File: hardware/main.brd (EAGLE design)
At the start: 95.2 x 80.4 mm, 96 parts, among them IC1 MPU-6050, IC2 TB6612FNG, M1 MOTOR_MOUNT_V2, M2 LED_MOUNT, M3 LED_MOUNT, M4 LED_MOUNT, M5 LED_MOUNT, M6 LED_MOUNT, M7 LED_MOUNT, Q7 IRLML2244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

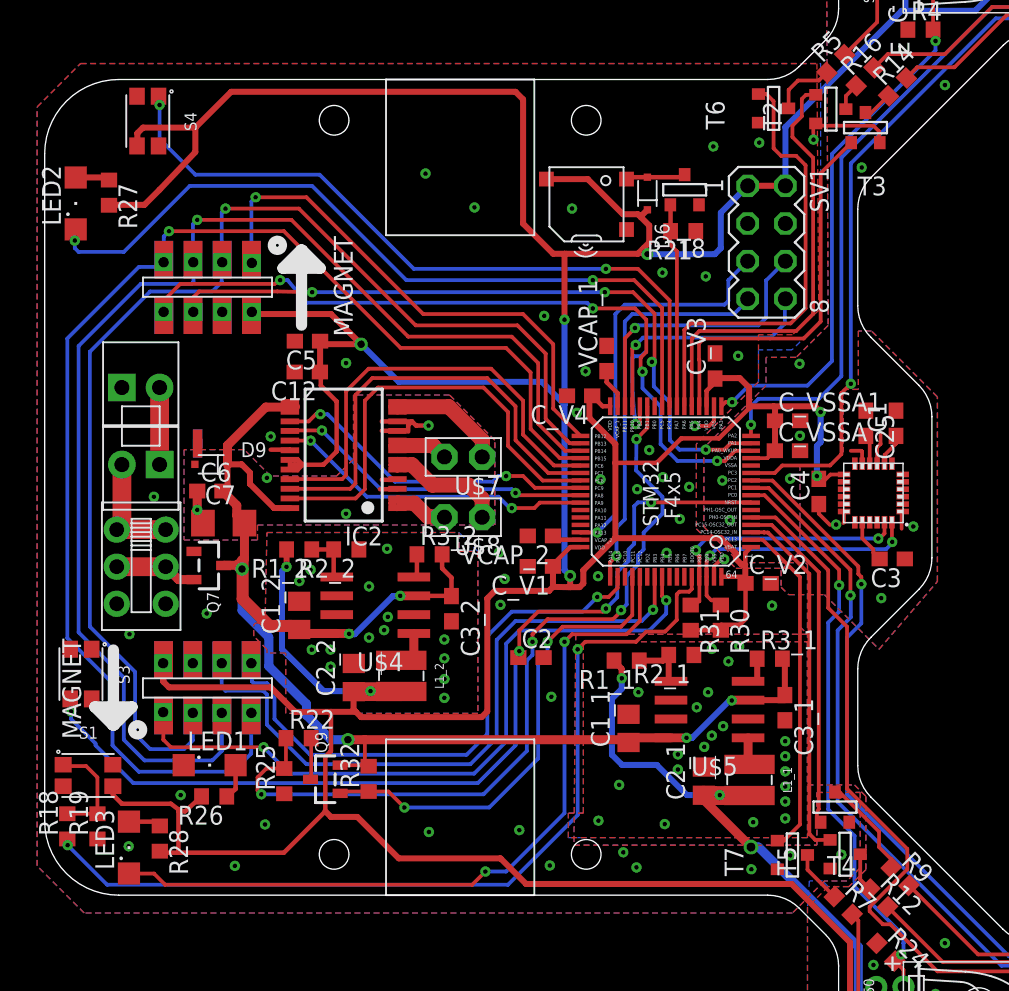
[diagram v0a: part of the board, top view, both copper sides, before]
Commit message: dodanie lini od przerwania od MPU, dodanie C na DCDC 3V3, laczenie GNDA GND i GNDM, dodanie diod ESD na programator, rewizja
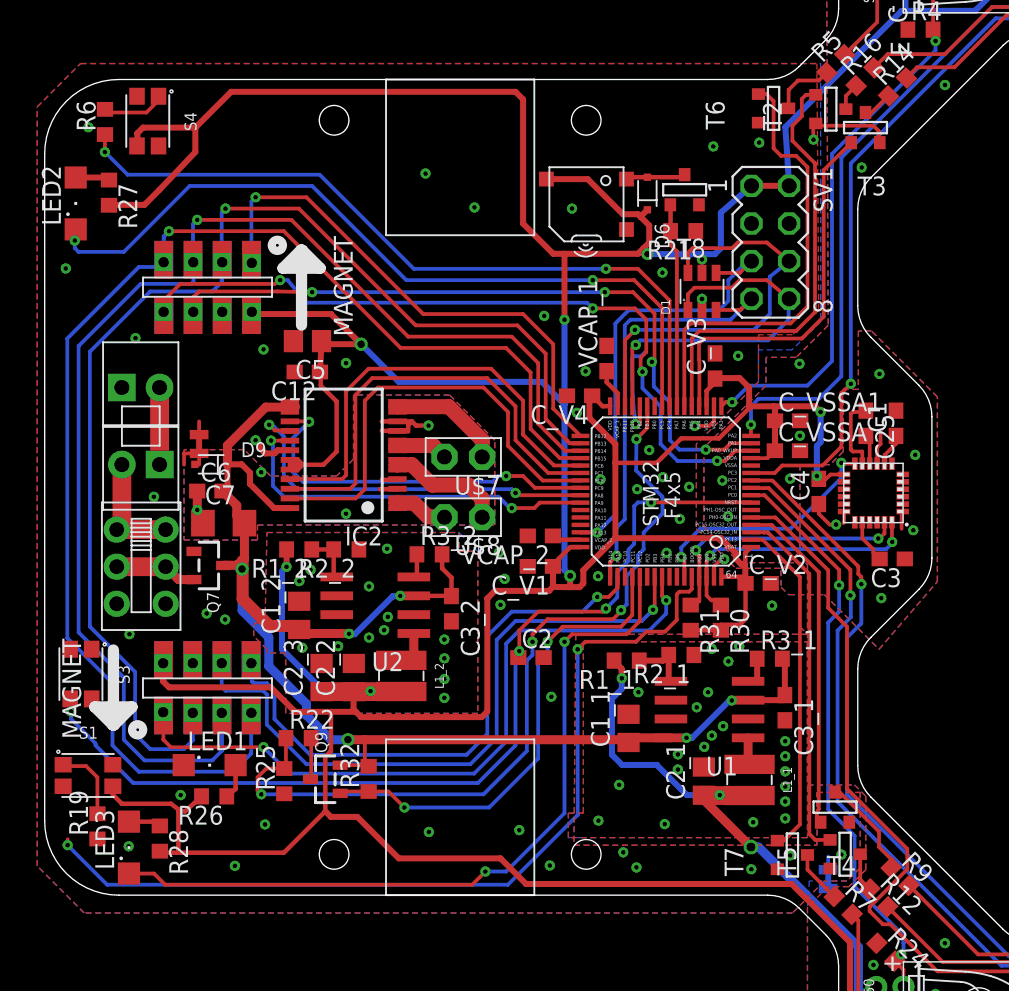
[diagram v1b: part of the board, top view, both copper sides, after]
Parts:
- removed R18: 1k, rcl:R0603
- removed U$1: GND_CONN, micromouse:GND_CONN
- added C2_3: 10u, rcl:C0805
- added D1: WE-TVS_824015, EAGLE-POWER_MAGNETICS-rev17a:WE-TVS_SOT23-6L
- added PT1, PT2: 2PT_GND_TIE, SparkFun-Passives:2PT_GND_TIE
- added R6: 1k, rcl:R0603
- C4: value 2,2n -> 100nF
- C5: device rcl:C0603 -> rcl:C0805
- moved SV1 0.25 mm to (48.9, 16.5)
- renumbered U$4 to U2, U$5 to U1, U$6 to U3
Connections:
- removed net N$23: R18.2, R19.2, S1.1
- removed net N$36: IC1.12
- removed net OSC_OUT: U3.PH1
- new net MPU_INT: IC1.12, U3.PB7
- new net N$25: R6.2, S4.1
- net +3V3: now also C2_3.1, D1.5
- net AGND: now also PT1.P$1
- net BOOT0: now also R19.2, S1.1; no longer R18.1
- net BTN1: now also R6.1; no longer S4.1
- net GND: now also C2_3.2, D1.2, PT1.P$2, PT2.P$1; no longer U$1.AGND, U$1.ANGD1
- net GNDA: now also PT2.P$2; no longer U$1.GND, U$1.GND1
- net SWCLK: now also D1.3
- net SWDIO: now also D1.4
- net USART3_RX: now also D1.6
- net USART3_TX: now also D1.1
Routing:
- net MPU_INT: track 0.00 -> 16.7 mm, vias 0 -> 2
- net USART3_TX: track 16.7 -> 25.8 mm
- net USART3_RX: track 19.0 -> 28.1 mm
- net GND: track 26.6 -> 34.5 mm, vias 83 -> 89
- net N$23: track 7.15 -> 0.00 mm
- net BOOT0: track 60.3 -> 65.3 mm
- net MR_IN2: track 21.4 -> 26.1 mm
- net MR_IN1: track 21.6 -> 26.0 mm
- net N$25: track 0.00 -> 4.29 mm
- net SWCLK: track 26.6 -> 30.8 mm
- net +3V3: track 514.5 -> 518.1 mm, vias 12 -> 13
- net MR_PWM: track 22.2 -> 25.3 mm
- net SWDIO: track 27.6 -> 30.2 mm
- net GNDA: track 9.93 -> 12.3 mm
- net SPI2_MOSI: track 89.0 -> 91.0 mm
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
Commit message: encoder lbr fix, connected gnd
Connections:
- net +3V3: now also U$10.8_2, U$9.8_2
- net ENCL_A: now also U$9.5_2
- net ENCL_B: now also U$9.6_2
- net ENCR_A: now also U$10.5_2
- net ENCR_B: now also U$10.6_2
- net GND: now also U$10.7_2, U$9.7_2
- net SPI2_CS1: now also U$9.1_2
- net SPI2_CS2: now also U$10.1_2
- net SPI2_MISO: now also U$10.3_2, U$9.3_2
- net SPI2_MOSI: now also U$10.4_2, U$9.4_2
- net SPI2_SCK: now also U$10.2_2, U$9.2_2
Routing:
- net BOOT0: track 65.3 -> 68.7 mm
- net SPI2_SCK: track 83.8 -> 82.5 mm
- net GND: vias 89 -> 90

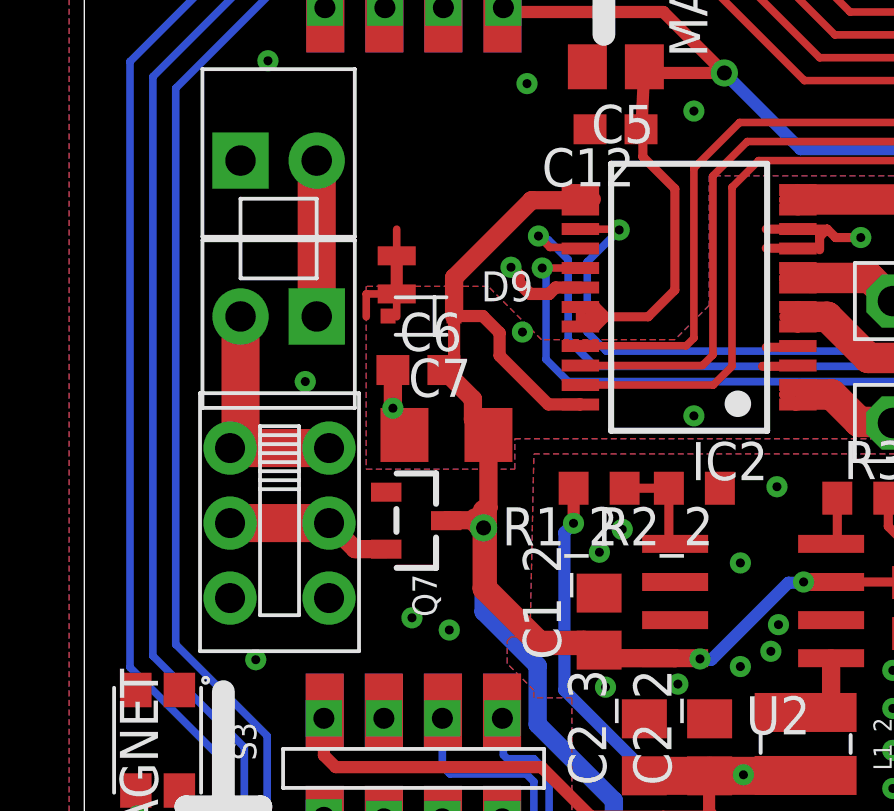
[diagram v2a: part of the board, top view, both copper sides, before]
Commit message: bugfix: mosfet przy zasilaniu
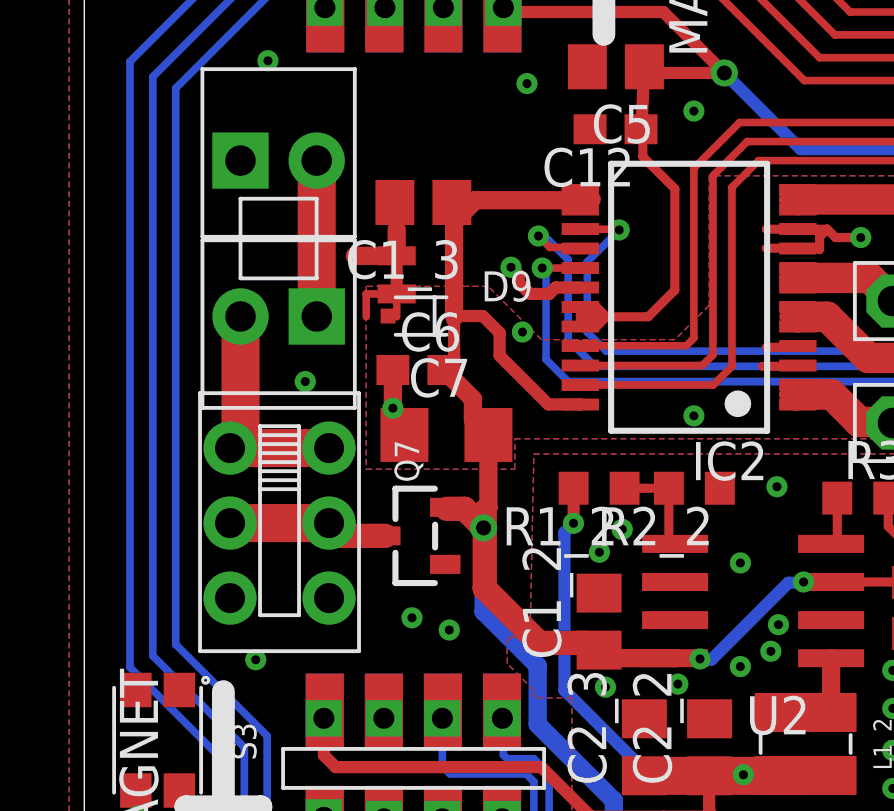
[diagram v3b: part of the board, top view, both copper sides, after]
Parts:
- added C1_3: 10u, rcl:C0805
- moved Q7 0.51 mm to (11.0, -5.78), turned to 90 degrees
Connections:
- net +7V: now also C1_3.1, Q7.2; no longer Q7.3
- net GND: now also C1_3.2
- net N$43: now also Q7.3; no longer Q7.2
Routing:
- net +7V: track 98.3 -> 100.0 mm
- net GND: track 34.5 -> 35.9 mm
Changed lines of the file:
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@@
 <layer number="25" name="tNames" color="7" fill="1" visible="yes" active="yes"/>
 <layer number="26" name="bNames" color="7" fill="1" visible="yes" active="yes"/>
-<layer number="27" name="tValues" color="7" fill="1" visible="yes" active="yes"/>
-<layer number="28" name="bValues" color="7" fill="1" visible="yes" active="yes"/>
+<layer number="27" name="tValues" color="7" fill="1" visible="no" active="yes"/>
+<layer number="28" name="bValues" color="7" fill="1" visible="no" active="yes"/>
 <layer number="29" name="tStop" color="7" fill="3" visible="no" active="yes"/>
 <layer number="30" name="bStop" color="7" fill="6" visible="no" active="yes"/>
@@
 <element name="IC1" library="invensense" package="QFN.24.4X4" value="MPU-6050" x="55.88" y="-0.381" rot="R180"/>
 <element name="IC2" library="_microMouse" package="SSOP24" value="TB6612FNG" x="20.161" y="2.175" rot="R90"/>
-<element name="Q7" library="microbuilder" package="SOT23-R" value="IRLML2244" x="11.065" y="-5.271" rot="R270"/>
+<element name="Q7" library="microbuilder" package="SOT23-R" value="IRLML2244" x="11.033" y="-5.778" rot="R90"/>
 <element name="R1" library="rcl" package="R0603" value="1,8k" x="82.677" y="-20.066" rot="R135"/>
 <element name="R12" library="rcl" package="R0603" value="1R" x="56.2356" y="-27.686" rot="R315"/>
@@
 <element name="PT2" library="SparkFun-Passives" package="2PT_GND_TIE" value="2PT_GND_TIE" x="10.414" y="2.921" smashed="yes"/>
 <element name="D1" library="EAGLE-POWER_MAGNETICS-rev17a" package="WE-TVS_SOT23-6L" value="WE-TVS_824015" x="44.323" y="13.208"/>
+<element name="C1_3" library="rcl" package="C0805" value="10u" x="11.303" y="5.334" rot="R180"/>
 </elements>
 <signals>
@@
 <contactref element="PT1" pad="P$2"/>
 <contactref element="PT2" pad="P$1"/>
-<wire x1="10.414" y1="3.556" x2="10.414" y2="4.445" width="0.254" layer="1"/>
 <wire x1="52.832" y1="-25.781" x2="52.832" y2="-24.892" width="0.254" layer="16"/>
 <contactref element="D1" pad="2"/>
@@
 <contactref element="U$9" pad="7_2"/>
 <contactref element="U$10" pad="7_2"/>
+<contactref element="C1_3" pad="2"/>
+<wire x1="10.414" y1="3.556" x2="10.414" y2="4.445" width="0.6096" layer="1"/>
+<wire x1="10.414" y1="3.556" x2="9.017" y2="3.556" width="0.6096" layer="1"/>
 </signal>
 <signal name="D_LS">
@@
 <signal name="N$43">
 <contactref element="ON" pad="2"/>
-<contactref element="Q7" pad="2"/>
 <contactref element="ON" pad="5"/>
 <wire x1="4.858" y1="-5.352" x2="8.158" y2="-5.352" width="1.27" layer="1"/>
-<wire x1="8.158" y1="-5.352" x2="9.027" y2="-6.221" width="0.6096" layer="1"/>
-<wire x1="9.027" y1="-6.221" x2="10.065" y2="-6.221" width="0.6096" layer="1"/>
+<contactref element="Q7" pad="3"/>
+<wire x1="8.158" y1="-5.352" x2="8.584" y2="-5.778" width="0.8128" layer="1"/>
+<wire x1="8.584" y1="-5.778" x2="10.033" y2="-5.778" width="0.8128" layer="1"/>
 </signal>
 <signal name="N$46">
@@
 <contactref element="U2" pad="3"/>
 <contactref element="C3_2" pad="1"/>
-<contactref element="Q7" pad="3"/>
 <contactref element="Q9" pad="2"/>
 <contactref element="R32" pad="2"/>
@@
 <contactref element="C7" pad="2"/>
 <contactref element="C6" pad="2"/>
-<wire x1="14.9098" y1="5.4102" x2="16.129" y2="5.4102" width="0.6096" layer="1"/>
 <contactref element="IC2" pad="14"/>
 <contactref element="IC2" pad="13"/>
 <contactref element="IC2" pad="24"/>
-<wire x1="12.065" y1="-5.271" x2="12.0782" y2="-5.2578" width="0.6096" layer="1"/>
-<wire x1="12.0782" y1="-5.2578" x2="13.0556" y2="-5.2578" width="0.6096" layer="1"/>
-<wire x1="13.0556" y1="-5.2578" x2="13.3477" y2="-4.9657" width="0.6096" layer="1"/>
 <wire x1="13.3477" y1="-4.9657" x2="13.4716" y2="-4.8418" width="0.6096" layer="1"/>
 <wire x1="13.4716" y1="-4.8418" x2="13.4716" y2="-2.415" width="0.6096" layer="1"/>
-<wire x1="13.0556" y1="-5.2578" x2="13.3096" y2="-5.5118" width="0.8128" layer="1"/>
 <wire x1="19.694" y1="-9.856" x2="19.6932" y2="-9.8552" width="0.6096" layer="1"/>
 <wire x1="19.6932" y1="-9.8552" x2="17.4302" y2="-9.8552" width="0.6096" layer="1"/>
@@
 <wire x1="49.911" y1="-14.351" x2="49.911" y2="-14.009" width="0.4064" layer="1"/>
 <contactref element="D9" pad="1"/>
-<wire x1="14.9098" y1="5.4102" x2="12.3268" y2="2.8272" width="0.6096" layer="1"/>
-<wire x1="12.3268" y1="2.8272" x2="12.3268" y2="1.5494" width="0.6096" layer="1"/>
 <wire x1="16.536" y1="-1.4" x2="16.533" y2="-1.397" width="0.4064" layer="1"/>
 <wire x1="16.533" y1="-1.397" x2="15.4686" y2="-1.397" width="0.4064" layer="1"/>
@@
 <wire x1="19.923" y1="-18.735" x2="21.844" y2="-18.735" width="0.254" layer="1"/>
 <wire x1="21.844" y1="-18.735" x2="21.844" y2="-18.8096" width="0.254" layer="1"/>
+<contactref element="Q7" pad="2"/>
+<wire x1="12.0782" y1="-4.8768" x2="12.6746" y2="-4.8768" width="0.8128" layer="1"/>
+<wire x1="12.6746" y1="-4.8768" x2="13.3096" y2="-5.5118" width="0.8128" layer="1"/>
+<contactref element="C1_3" pad="1"/>
+<wire x1="12.253" y1="5.334" x2="12.253" y2="5.146" width="0.6096" layer="1"/>
+<wire x1="12.3268" y1="1.5494" x2="12.3268" y2="4.699" width="0.6096" layer="1"/>
+<wire x1="12.3268" y1="4.699" x2="12.3268" y2="5.1332" width="0.6096" layer="1"/>
+<wire x1="12.3268" y1="5.1332" x2="12.253" y2="5.334" width="0.6096" layer="1"/>
+<wire x1="16.129" y1="5.4102" x2="13.038" y2="5.4102" width="0.6096" layer="1"/>
+<wire x1="13.038" y1="5.4102" x2="12.3268" y2="4.699" width="0.6096" layer="1"/>
+<wire x1="12.0782" y1="-4.8768" x2="12.033" y2="-4.828" width="0" layer="19" extent="1-1"/>
+<wire x1="13.3477" y1="-4.9657" x2="13.3096" y2="-5.5118" width="0" layer="19" extent="1-1"/>
 </signal>
 <signal name="N$52">

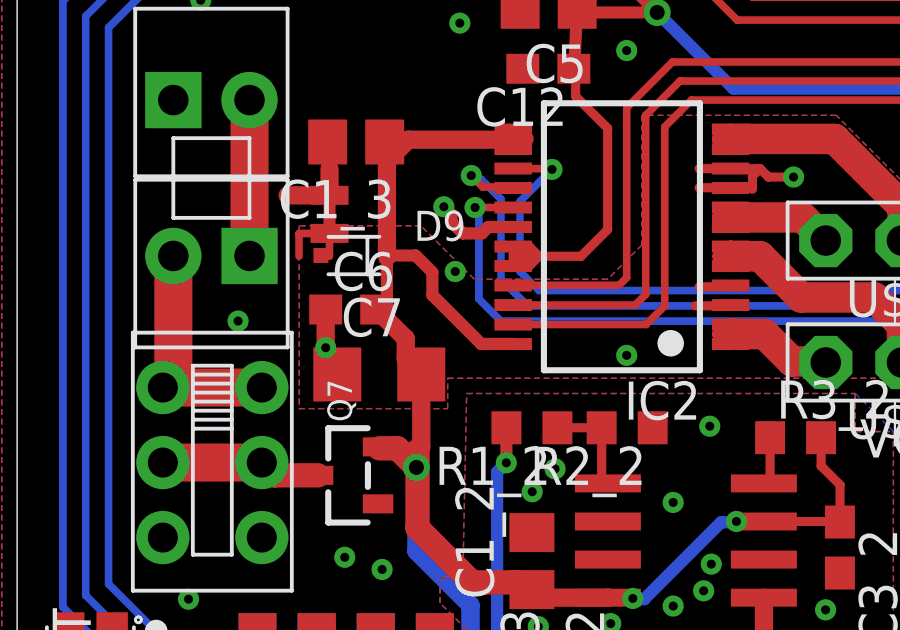
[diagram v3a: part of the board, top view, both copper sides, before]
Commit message: poprawa 1 sciezki przy bateii
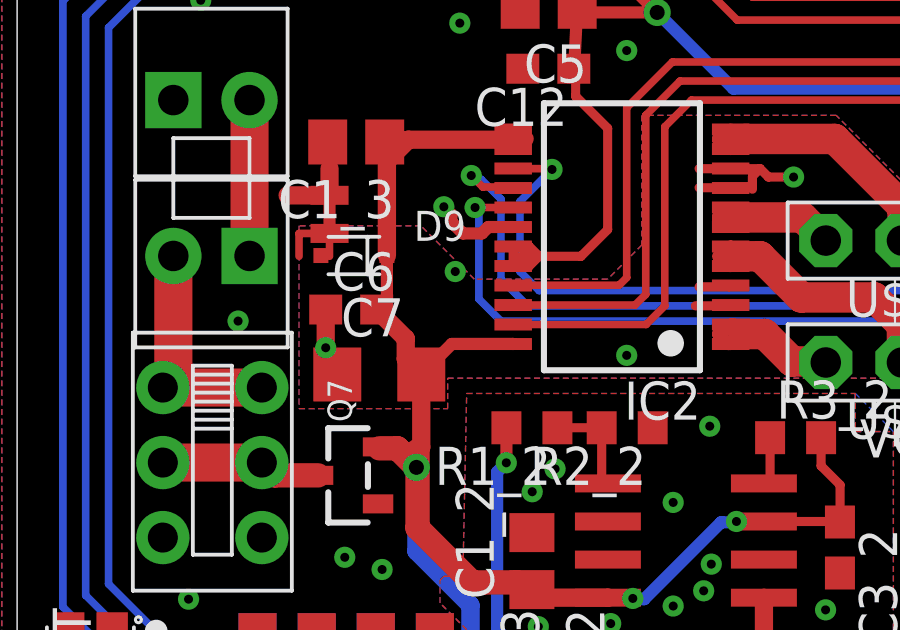
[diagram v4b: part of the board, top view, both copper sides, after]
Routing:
- net +7V: track 100.0 -> 97.6 mm
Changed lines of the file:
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@@
 <contactref element="D9" pad="1"/>
 <wire x1="16.536" y1="-1.4" x2="16.533" y2="-1.397" width="0.4064" layer="1"/>
-<wire x1="16.533" y1="-1.397" x2="15.4686" y2="-1.397" width="0.4064" layer="1"/>
-<wire x1="15.4686" y1="-1.397" x2="13.843" y2="0.2286" width="0.4064" layer="1"/>
-<wire x1="13.843" y1="0.2286" x2="13.843" y2="0.9906" width="0.4064" layer="1"/>
-<wire x1="13.843" y1="0.9906" x2="13.2842" y2="1.5494" width="0.4064" layer="1"/>
-<wire x1="13.2842" y1="1.5494" x2="12.3268" y2="1.5494" width="0.4064" layer="1"/>
 <wire x1="11.9864" y1="-0.251" x2="12.3268" y2="0.0894" width="0.4064" layer="1"/>
 <wire x1="12.3268" y1="0.0894" x2="12.3268" y2="1.5494" width="0.4064" layer="1"/>
@@
 <wire x1="16.129" y1="5.4102" x2="13.038" y2="5.4102" width="0.6096" layer="1"/>
 <wire x1="13.038" y1="5.4102" x2="12.3268" y2="4.699" width="0.6096" layer="1"/>
+<wire x1="16.533" y1="-1.397" x2="14.4896" y2="-1.397" width="0.4064" layer="1"/>
+<wire x1="14.4896" y1="-1.397" x2="13.4716" y2="-2.415" width="0.4064" layer="1"/>
 <wire x1="12.0782" y1="-4.8768" x2="12.033" y2="-4.828" width="0" layer="19" extent="1-1"/>
 <wire x1="13.3477" y1="-4.9657" x2="13.3096" y2="-5.5118" width="0" layer="19" extent="1-1"/>
